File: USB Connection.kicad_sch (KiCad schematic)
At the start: 2 parts, among them J1 USB_A, P2 USB_C_Plug_USB2.0

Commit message: Finished capturing schematics
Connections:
- net GND renamed GND USB
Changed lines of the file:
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@@
 	(symbol
 		(lib_id "power:Earth")
-		(at 139.7 106.68 0)
-		(unit 1)
-		(exclude_from_sim no)
-		(in_bom yes)
-		(on_board yes)
-		(dnp no)
-		(fields_autoplaced yes)
-		(property "Reference" "#PWR04"
-			(at 139.7 113.03 0)
-			(effects
-				(font
-					(size 1.27 1.27)
-				)
-				(hide yes)
-			)
-		)
-		(property "Value" "GND"
-			(at 139.7 111.76 0)
-			(effects
-				(font
-					(size 1.27 1.27)
-				)
-			)
-		)
-		(property "Footprint" ""
-			(at 139.7 106.68 0)
+		(at 139.7 144.78 0)
+		(unit 1)
+		(exclude_from_sim no)
+		(in_bom yes)
+		(on_board yes)
+		(dnp no)
+		(fields_autoplaced yes)
+		(property "Reference" "#PWR01"
+			(at 139.7 151.13 0)
+			(effects
+				(font
+					(size 1.27 1.27)
+				)
+				(hide yes)
+			)
+		)
+		(property "Value" "GND USB"
+			(at 139.7 149.86 0)
+			(effects
+				(font
+					(size 1.27 1.27)
+				)
+			)
+		)
+		(property "Footprint" ""
+			(at 139.7 144.78 0)
 			(effects
 				(font
@@
 		)
 		(property "Datasheet" "~"
-			(at 139.7 106.68 0)
+			(at 139.7 144.78 0)
 			(effects
 				(font
@@
 		)
 		(property "Description" "Power symbol creates a global label with name \"Earth\""
-			(at 139.7 106.68 0)
+			(at 139.7 144.78 0)
 			(effects
 				(font
@@
 			(project "Isolated Com Port"
 				(path "/736fe05f-3e80-4c58-a4b9-c0a7b5ae4e97/ee1179b6-f3bc-4588-883b-b016ef356bec"
-					(reference "#PWR04")
+					(reference "#PWR01")
 					(unit 1)
 				)
@@
 	(symbol
 		(lib_id "power:Earth")
-		(at 139.7 144.78 0)
-		(unit 1)
-		(exclude_from_sim no)
-		(in_bom yes)
-		(on_board yes)
-		(dnp no)
-		(fields_autoplaced yes)
-		(property "Reference" "#PWR01"
-			(at 139.7 151.13 0)
-			(effects
-				(font
-					(size 1.27 1.27)
-				)
-				(hide yes)
-			)
-		)
-		(property "Value" "GND"
-			(at 139.7 149.86 0)
-			(effects
-				(font
-					(size 1.27 1.27)
-				)
-			)
-		)
-		(property "Footprint" ""
-			(at 139.7 144.78 0)
+		(at 139.7 106.68 0)
+		(unit 1)
+		(exclude_from_sim no)
+		(in_bom yes)
+		(on_board yes)
+		(dnp no)
+		(fields_autoplaced yes)
+		(property "Reference" "#PWR04"
+			(at 139.7 113.03 0)
+			(effects
+				(font
+					(size 1.27 1.27)
+				)
+				(hide yes)
+			)
+		)
+		(property "Value" "GND USB"
+			(at 139.7 111.76 0)
+			(effects
+				(font
+					(size 1.27 1.27)
+				)
+			)
+		)
+		(property "Footprint" ""
+			(at 139.7 106.68 0)
 			(effects
 				(font
@@
 		)
 		(property "Datasheet" "~"
-			(at 139.7 144.78 0)
+			(at 139.7 106.68 0)
 			(effects
 				(font
@@
 		)
 		(property "Description" "Power symbol creates a global label with name \"Earth\""
-			(at 139.7 144.78 0)
+			(at 139.7 106.68 0)
 			(effects
 				(font
@@
 			(project "Isolated Com Port"
 				(path "/736fe05f-3e80-4c58-a4b9-c0a7b5ae4e97/ee1179b6-f3bc-4588-883b-b016ef356bec"
-					(reference "#PWR01")
-					(unit 1)
-				)
+					(reference "#PWR04")
+					(unit 1)
+				)

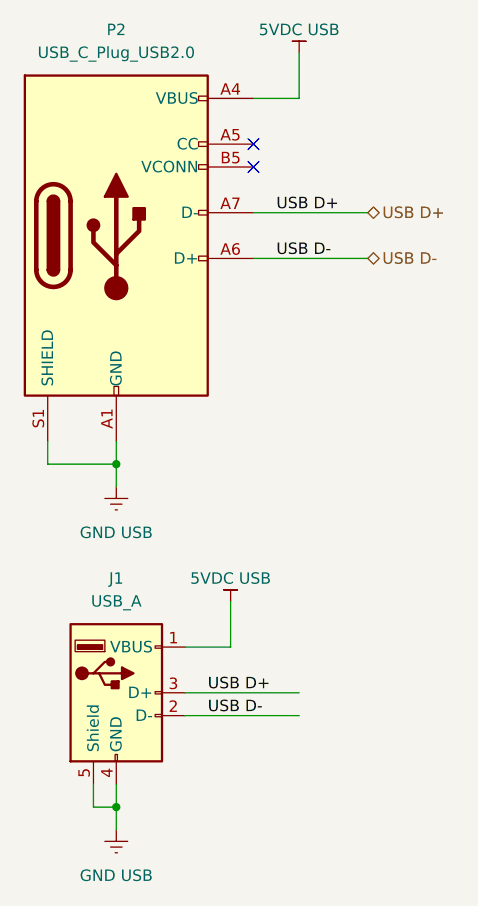
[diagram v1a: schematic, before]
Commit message: Power & Level Translation
Isolated 5VDC changed and a 3.3VDC LDO was added. The original 5VDC was too expensive and big. The new one is still both, but less so.
The level translator is now a dedicated IC instead of MOSFETs. I was having trouble making it work the way I wanted.
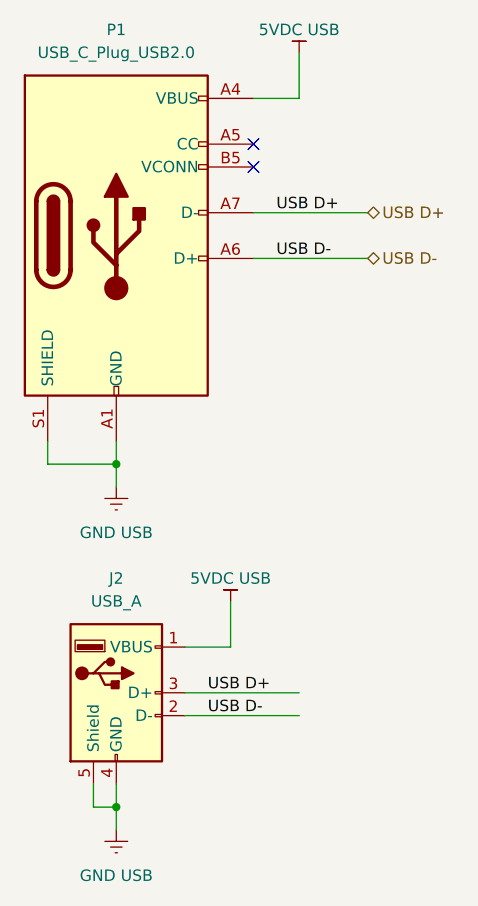
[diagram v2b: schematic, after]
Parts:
- renumbered J1 to J2, P2 to P1
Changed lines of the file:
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@@
 		(dnp no)
 		(fields_autoplaced yes)
-		(property "Reference" "#PWR01"
+		(property "Reference" "#PWR06"
 			(at 139.7 151.13 0)
 			(effects
@@
 			(project "Isolated Com Port"
 				(path "/736fe05f-3e80-4c58-a4b9-c0a7b5ae4e97/ee1179b6-f3bc-4588-883b-b016ef356bec"
-					(reference "#PWR01")
+					(reference "#PWR06")
 					(unit 1)
 				)
@@
 		(dnp no)
 		(fields_autoplaced yes)
-		(property "Reference" "#PWR03"
+		(property "Reference" "#PWR08"
 			(at 160.02 62.23 0)
 			(effects
@@
 			(project "Isolated Com Port"
 				(path "/736fe05f-3e80-4c58-a4b9-c0a7b5ae4e97/ee1179b6-f3bc-4588-883b-b016ef356bec"
-					(reference "#PWR03")
+					(reference "#PWR08")
 					(unit 1)
 				)
@@
 		(dnp no)
 		(fields_autoplaced yes)
-		(property "Reference" "J1"
+		(property "Reference" "J2"
 			(at 139.7 116.84 0)
 			(effects
@@
 			(project "Isolated Com Port"
 				(path "/736fe05f-3e80-4c58-a4b9-c0a7b5ae4e97/ee1179b6-f3bc-4588-883b-b016ef356bec"
-					(reference "J1")
+					(reference "J2")
 					(unit 1)
 				)
@@
 		(dnp no)
 		(fields_autoplaced yes)
-		(property "Reference" "P2"
+		(property "Reference" "P1"
 			(at 139.7 55.88 0)
 			(effects
@@
 			(project "Isolated Com Port"
 				(path "/736fe05f-3e80-4c58-a4b9-c0a7b5ae4e97/ee1179b6-f3bc-4588-883b-b016ef356bec"
-					(reference "P2")
+					(reference "P1")
 					(unit 1)
 				)
@@
 		(dnp no)
 		(fields_autoplaced yes)
-		(property "Reference" "#PWR02"
+		(property "Reference" "#PWR07"
 			(at 152.4 123.19 0)
 			(effects
@@
 			(project "Isolated Com Port"
 				(path "/736fe05f-3e80-4c58-a4b9-c0a7b5ae4e97/ee1179b6-f3bc-4588-883b-b016ef356bec"
-					(reference "#PWR02")
+					(reference "#PWR07")
 					(unit 1)
 				)
@@
 		(dnp no)
 		(fields_autoplaced yes)
-		(property "Reference" "#PWR04"
+		(property "Reference" "#PWR05"
 			(at 139.7 113.03 0)
 			(effects
@@
 			(project "Isolated Com Port"
 				(path "/736fe05f-3e80-4c58-a4b9-c0a7b5ae4e97/ee1179b6-f3bc-4588-883b-b016ef356bec"
-					(reference "#PWR04")
-					(unit 1)
-				)
+					(reference "#PWR05")
+					(unit 1)
+				)
